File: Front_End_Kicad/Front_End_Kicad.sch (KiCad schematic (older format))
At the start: 1 part, among them U101 AD628

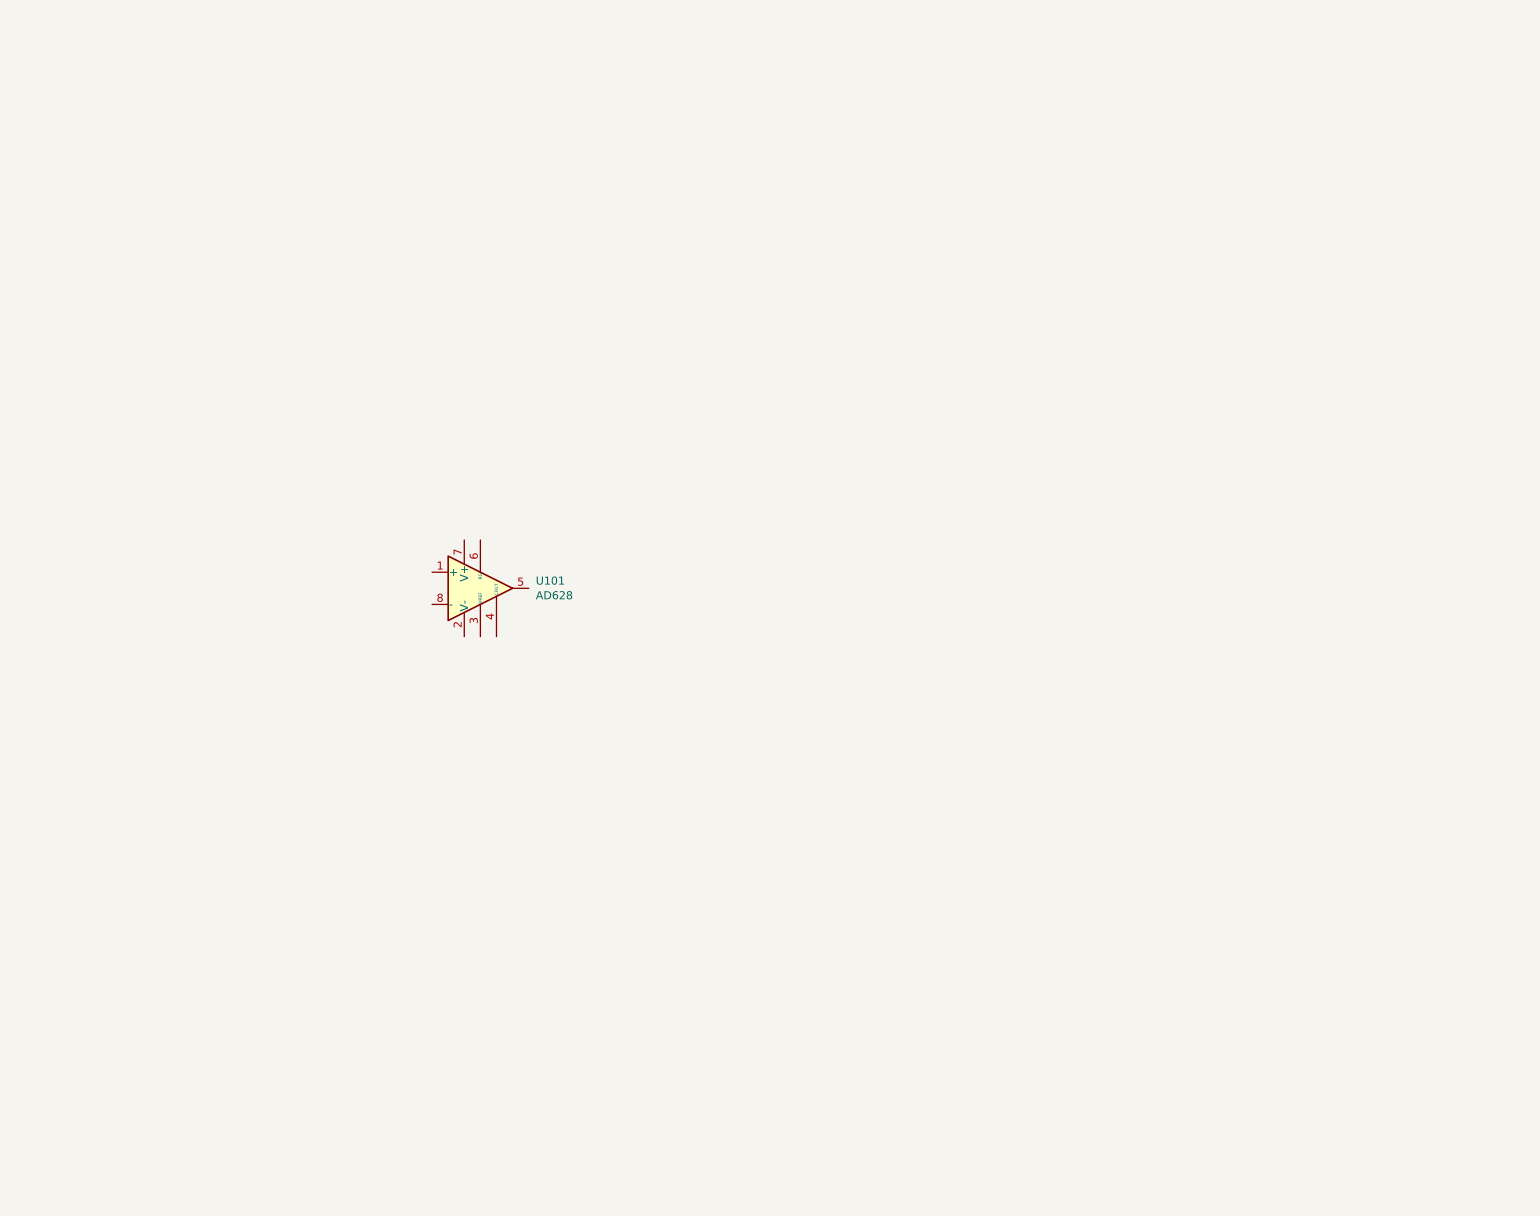
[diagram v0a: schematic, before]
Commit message: Some work here and there.  Opamp selected and 1 voltage driver selected.
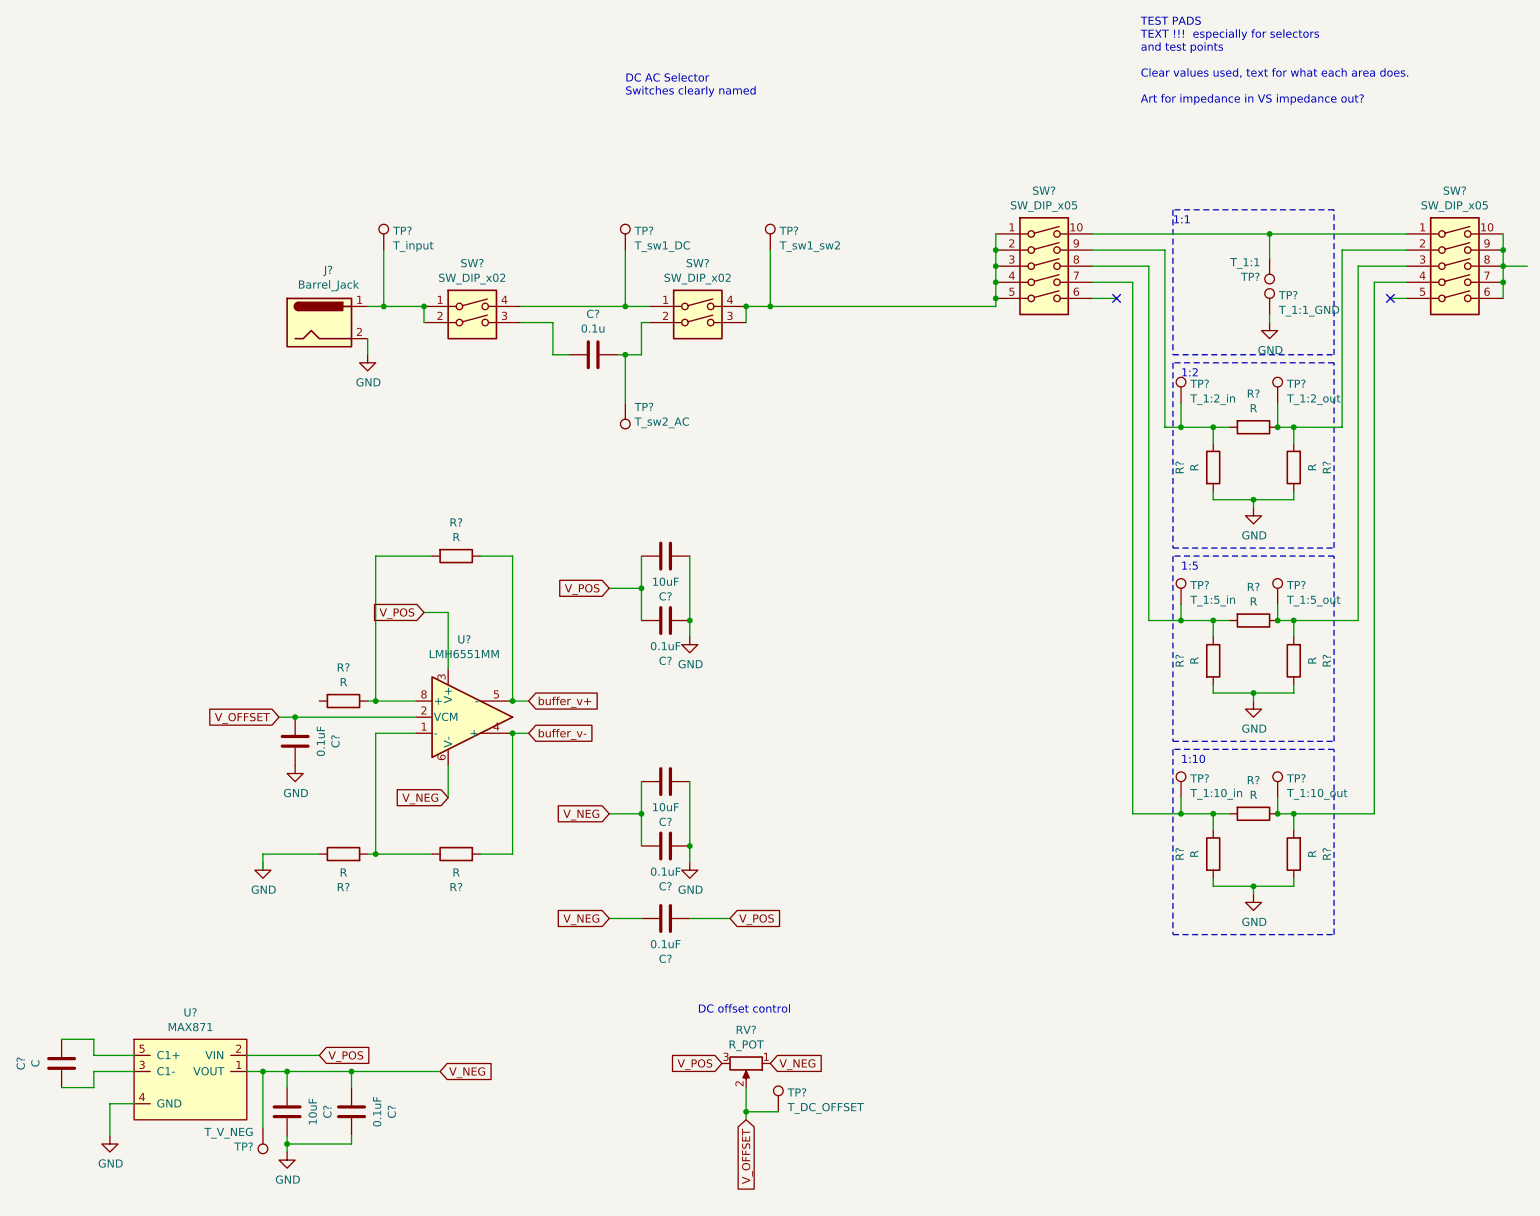
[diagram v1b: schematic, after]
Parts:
- removed U101: AD628, symbol Amplifier_Difference:AD628
- added C?: 0.1u, symbol Device:C
- added C? (x3): 10uF, symbol Device:C
- added C?: C, symbol Device:C
- added C? (x5): 0.1uF, symbol Device:C
- added J?: Barrel_Jack, symbol Connector:Barrel_Jack
- added R? (x13): R, symbol Device:R
- added RV?: R_POT, Front_End_Kicad:Senior_Design_Front_End, symbol Device:R_POT
- added SW? (x2): SW_DIP_x02, Package_DIP:DIP-4_W7.62mm, symbol Switch:SW_DIP_x02
- added SW? (x2): SW_DIP_x05, Package_DIP:DIP-10_W7.62mm, symbol Switch:SW_DIP_x05
- added TP?: T_input, symbol Connector:TestPoint
- added TP?: T_sw1_DC, symbol Connector:TestPoint
- added TP?: T_sw2_AC, symbol Connector:TestPoint
- added TP?: T_sw1_sw2, symbol Connector:TestPoint
- added TP?: T_1:1, symbol Connector:TestPoint
- added TP?: T_1:2_in, symbol Connector:TestPoint
- added TP?: T_1:2_out, symbol Connector:TestPoint
- added TP?: T_1:5_in, symbol Connector:TestPoint
- added TP?: T_1:5_out, symbol Connector:TestPoint
- added TP?: T_1:10_in, symbol Connector:TestPoint
- added TP?: T_1:10_out, symbol Connector:TestPoint
- added TP?: T_V_NEG, symbol Connector:TestPoint
- added TP?: T_1:1_GND, symbol Connector:TestPoint
- added TP?: T_DC_OFFSET, symbol Connector:TestPoint
- added U?: MAX871, symbol Front_End_Symbol_Lib:MAX871
- added U?: LMH6551MM, Package_SO:VSSOP-8_3.0x3.0mm_P0.65mm, symbol Amplifier_Operational:LMH6551MM
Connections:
- new net: J?.1, SW?.1, SW?.2, TP?.1
- new net: C?.1, SW?.3
- new net: SW?.1, SW?.4, TP?.1
- new net: C?.2, SW?.2, TP?.1
- new net: SW?.1, SW?.2, SW?.3, SW?.3, SW?.4, SW?.4, SW?.5, TP?.1
- new net: SW?.1, SW?.10, TP?.1
- new net: R?.1, R?.2, SW?.7, TP?.1
- new net: R?.1, R?.2, SW?.8, TP?.1
- new net: R?.1, R?.2, SW?.9, TP?.1
- new net: SW?.10, SW?.6, SW?.7, SW?.8, SW?.9
- new net: R?.1, R?.2, SW?.2, TP?.1
- new net: R?.1, R?.2, SW?.3, TP?.1
- new net: R?.1, R?.2, SW?.4, TP?.1
- new net: C?.1, U?.3 (C1-)
- new net: C?.2, U?.5 (C1+)
- new net: R?.1, R?.2, U?.1 (-)
- new net: R?.1, R?.2, U?.8 (+)
- new net GND: C?.1, C?.1, C?.1, C?.1, C?.2, C?.2, C?.2, J?.2, R?.1, R?.1, R?.1, R?.2, R?.2, R?.2, TP?.1, U?.4 (GND)
- new net V_NEG: C?.1, C?.1, C?.2, C?.2, C?.2, RV?.1, TP?.1, U?.1 (VOUT), U?.6 (V-)
- new net V_OFFSET: C?.1, RV?.2, TP?.1, U?.2 (VCM)
- new net V_POS: C?.1, C?.2, C?.2, RV?.3, U?.2 (VIN), U?.3 (V+)
- new net buffer_v+: R?.1, U?.5 (-)
- new net buffer_v-: R?.2, U?.4 (+)
- no-connect marks 0 -> 2
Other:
- note added: "1:10"
- note added: "1:1\n"
- note added: "1:2"
- note added: "1:5"
- note added: "DC AC Selector\nSwitches clearly named"
- note added: "DC offset control\n"
- note added: "TEST PADS\nTEXT !!! especially for selectors\nand test points\n\nClear values used, text for what each area does.\n\nArt for impedance in VS impedance out?"

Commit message: Split powre system off. Small devolopment with notes and layout.
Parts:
- removed C?: 10uF, symbol Device:C
- removed C?: C, symbol Device:C
- removed C?: 0.1uF, symbol Device:C
- removed R? (x9): R, symbol Device:R
- removed RV?: R_POT, Front_End_Kicad:Senior_Design_Front_End, symbol Device:R_POT
- removed TP?: T_input, symbol Connector:TestPoint
- removed TP?: T_sw1_DC, symbol Connector:TestPoint
- removed TP?: T_sw1_sw2, symbol Connector:TestPoint
- removed TP?: T_1:1, symbol Connector:TestPoint
- removed TP?: T_1:2_in, symbol Connector:TestPoint
- removed TP?: T_1:2_out, symbol Connector:TestPoint
- removed TP?: T_1:5_in, symbol Connector:TestPoint
- removed TP?: T_1:5_out, symbol Connector:TestPoint
- removed TP?: T_1:10_in, symbol Connector:TestPoint
- removed TP?: T_1:10_out, symbol Connector:TestPoint
- removed TP?: T_V_NEG, symbol Connector:TestPoint
- removed TP?: T_1:1_GND, symbol Connector:TestPoint
- removed TP?: T_DC_OFFSET, symbol Connector:TestPoint
- removed U?: MAX871, symbol Front_End_Symbol_Lib:MAX871
- added R? (x12): R, symbol Device:R
- added TP?: attn_2x, TestPoint:TestPoint_2Pads_Pitch5.08mm_Drill1.3mm, symbol Connector:TestPoint_2Pole
- added TP?: attn_2x_gnd, TestPoint:TestPoint_2Pads_Pitch5.08mm_Drill1.3mm, symbol Connector:TestPoint
- added TP?: attn_5x, symbol Connector:TestPoint_2Pole
- added TP?: attn_5x_gnd, TestPoint:TestPoint_THTPad_3.0x3.0mm_Drill1.5mm, symbol Connector:TestPoint
- added TP?: attn_10x, TestPoint:TestPoint_2Pads_Pitch5.08mm_Drill1.3mm, symbol Connector:TestPoint_2Pole
- added TP?: attn_10x_gnd, TestPoint:TestPoint_THTPad_3.0x3.0mm_Drill1.5mm, symbol Connector:TestPoint
- added TP?: attn_20x, TestPoint:TestPoint_2Pads_Pitch5.08mm_Drill1.3mm, symbol Connector:TestPoint_2Pole
- added TP?: attn_20x_gnd, TestPoint:TestPoint_THTPad_3.0x3.0mm_Drill1.5mm, symbol Connector:TestPoint
- added TP?: buffer_diff, symbol Connector:TestPoint_2Pole
- added TP? (x2): buff_diff_gnd, TestPoint:TestPoint_THTPad_3.0x3.0mm_Drill1.5mm, symbol Connector:TestPoint
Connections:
- net GND: now also C?.2, C?.2, R?.1, R?.1, R?.1, R?.1, R?.1, R?.2, R?.2, R?.2, R?.2, TP?.1, TP?.1, TP?.1, TP?.1, TP?.1; no longer C?.1, C?.1
- net buffer_v+: now also TP?.2
- net buffer_v-: now also TP?.1
- net at SW?.3: now also C?.2; no longer C?.1
- net at SW?.2, TP?.1: now also C?.1; no longer C?.2
- net attenuation_1x_in: now reaches SW?.1, SW?.10
- net attenuation_20x_in: now reaches SW?.6
- net attenuation_20x_in: now also R?.1, R?.2, TP?.1
- net attenuation_10x_in: now reaches SW?.7
- net attenuation_10x_in: now also R?.1, R?.2, TP?.1
- net attenuation_5x_in: now reaches SW?.8
- net attenuation_5x_in: now also R?.1, R?.2, TP?.1
- net attenuation_2x_in: now reaches SW?.9
- net attenuation_2x_in: now also R?.1, R?.2, TP?.1
- net attenuation_2x_out: now reaches SW?.2
- net attenuation_2x_out: now also R?.1, R?.2, TP?.2
- net attenuation_5x_out: now reaches SW?.3
- net attenuation_5x_out: now also R?.1, R?.2, TP?.2
- net attenuation_10x_out: now reaches SW?.4
- net attenuation_10x_out: now also R?.1, R?.2, TP?.2
- net attenuation_20x_out: now reaches SW?.5
- net attenuation_20x_out: now also R?.1, R?.2, TP?.2
- removed net V_NEG: C?.2, C?.2, C?.2, U?.6 (V-)
- net V_POS renamed V_+5v
- net V_+5v: now also C?.2; no longer C?.1
- new net V_-5v: C?.1, C?.1, C?.1, U?.6 (V-)
- no-connect marks 2 -> 0
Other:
- note added: "Buffer bypass"
- note removed: "1:10"
- note removed: "1:1\n"
- note removed: "1:2"
- note removed: "1:5"
- note removed: "DC offset control\n"
- moved on the sheet: C?, J?, R?, SW?, TP?, U?

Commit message: Added footprints and digikey links to many of the components.  Missing is the primary amplifier
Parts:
- removed C?: 0.1u, symbol Device:C
- removed C? (x3): 0.1uF, symbol Device:C
- removed R? (x4): R, symbol Device:R
- added C101, C103, C106, C107: 0.1uF, Capacitor_SMD:C_1206_3216Metric, symbol Device:C
- added R113: 150, Resistor_SMD:R_1206_3216Metric, symbol Device:R
- added R114: 75, Resistor_SMD:R_1206_3216Metric, symbol Device:R
- added R115: 60.4, Resistor_SMD:R_1206_3216Metric, symbol Device:R
- added R116: 54.9, Resistor_SMD:R_1206_3216Metric, symbol Device:R
- C102, C105: renamed from C?; footprint (none) -> Capacitor_SMD:C_1206_3216Metric; part_url (none) -> https://www.digikey.com/en/products/detail/taiyo-yuden/EMK3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
- C104: renamed from C?; footprint (none) -> Capacitor_SMD:C_1206_3216Metric; part_url (none) -> https://www.digikey.com/en/products/detail/w%C3%BCrth-elekt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
- J101: renamed from J?; footprint (none) -> Connector_Coaxial:BNC_Amphenol_B6252HB-NPP3G-50_Horizontal; part_description TODO ACTUALLY TEST THIS -> (none)
- R101, R102, R103, R104: renamed from R?; footprint (none) -> Resistor_SMD:R_1206_3216Metric
- R105: renamed from R?; value R -> 150; footprint (none) -> Resistor_SMD:R_1206_3216Metric; part_url (none) -> https://www.digikey.com/en/products/detail/stackpole-electr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
- R106: renamed from R?; value R -> 75; footprint (none) -> Resistor_SMD:R_1206_3216Metric; part_url (none) -> https://www.digikey.com/en/products/detail/stackpole-electr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
- R107: renamed from R?; value R -> 60.4; footprint (none) -> Resistor_SMD:R_1206_3216Metric; part_url (none) -> https://www.digikey.com/en/products/detail/stackpole-electr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
- R108: renamed from R?; value R -> 54.9; footprint (none) -> Resistor_SMD:R_1206_3216Metric; part_url (none) -> https://www.digikey.com/en/products/detail/panasonic-electr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
- R109: renamed from R?; value R -> 37.4; footprint (none) -> Resistor_SMD:R_1206_3216Metric; part_url (none) -> https://www.digikey.com/en/products/detail/yageo/RC1206FR-0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
- R110: renamed from R?; value R -> 120; footprint (none) -> Resistor_SMD:R_1206_3216Metric; part_url (none) -> https://www.digikey.com/en/products/detail/stackpole-electr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
- R111: renamed from R?; value R -> 249; footprint (none) -> Resistor_SMD:R_1206_3216Metric; part_url (none) -> https://www.digikey.com/en/products/detail/stackpole-electr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
- R112: renamed from R?; value R -> 499; footprint (none) -> Resistor_SMD:R_1206_3216Metric; part_url (none) -> https://www.digikey.com/en/products/detail/stackpole-electr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
- TP102: renamed from TP?; footprint (none) -> TestPoint:TestPoint_THTPad_3.0x3.0mm_Drill1.5mm
- TP103, TP106: renamed from TP?; footprint (none) -> TestPoint:TestPoint_2Pads_Pitch5.08mm_Drill1.3mm
- gave numbers to parts that had none: 14
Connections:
- net GND: now also C101.2, C103.1, C106.2, R113.1, R114.1, R115.1, R116.1
- net V_+5v: now also C103.2
- net V_-5v: now also C106.1
- net attenuation_10x_out: now also R115.2
- net attenuation_20x_out: now also R116.2
- net attenuation_2x_out: now also R113.2
- net attenuation_5x_out: now also R114.2
- net at SW101.3: now also C107.2
- net at SW102.2, TP102.1: now also C107.1
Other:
- note added: "R1 : L and R"
- note added: "R1: -55.28 Ω\nR2: -497.6 Ω"
- note added: "R1: -61.11 Ω\nR2: -247.5 Ω"
- note added: "R1: -74.93 Ω\nR2: -120.3 Ω"
- note added: "\nR1: -150.5 Ω\nR2: -37.35 Ω"
